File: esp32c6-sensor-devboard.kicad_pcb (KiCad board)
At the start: 4 copper layers, 90 x 50 mm, 183 parts, among them J1 Conn_01x04_Pin, J2 Micro_SD_Card_Det1, J3 Screw_Terminal_01x02, J4 USB_C_Receptacle_USB2.0_14P, J5 Screw_Terminal_01x02, J6 Screw_Terminal_01x06, J7 Screw_Terminal_01x04, J8 Conn_01x04_Pin, J9 Conn_01x03_Pin, SW1 SW_Push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

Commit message: pcb: add inner gnd planes
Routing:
- added copper zone on In1.Cu, net GND
- added copper zone on In2.Cu, net GND
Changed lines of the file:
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@@
+		)
+	)
+	(zone
+		(net 2)
+		(net_name "GND")
+		(layers "In1.Cu" "In2.Cu")
+		(hatch edge 0.5)
+		(connect_pads
+			(clearance 0.3)
+		)
+		(min_thickness 0.15)
+		(filled_areas_thickness no)
+		(fill yes
+			(thermal_gap 0.4)
+			(thermal_bridge_width 0.25)
+		)
+		(polygon
+			(pts
+				(xy 132 67) (xy 222 67) (xy 222 117) (xy 132 117)
+			)
 		)
 	)

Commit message: pcb: add tooling holes
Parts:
- added REF**: ToolingHole_1.152mm, MountingHole:ToolingHole_1.152mm, F.Cu at (216.0, 114.0)
- added REF**: ToolingHole_1.152mm, MountingHole:ToolingHole_1.152mm, F.Cu at (218.0, 70.0)
- added REF**: ToolingHole_1.152mm, MountingHole:ToolingHole_1.152mm, F.Cu at (151.0, 114.0)
- added REF**: ToolingHole_1.152mm, MountingHole:ToolingHole_1.152mm, F.Cu at (141.0, 75.0)

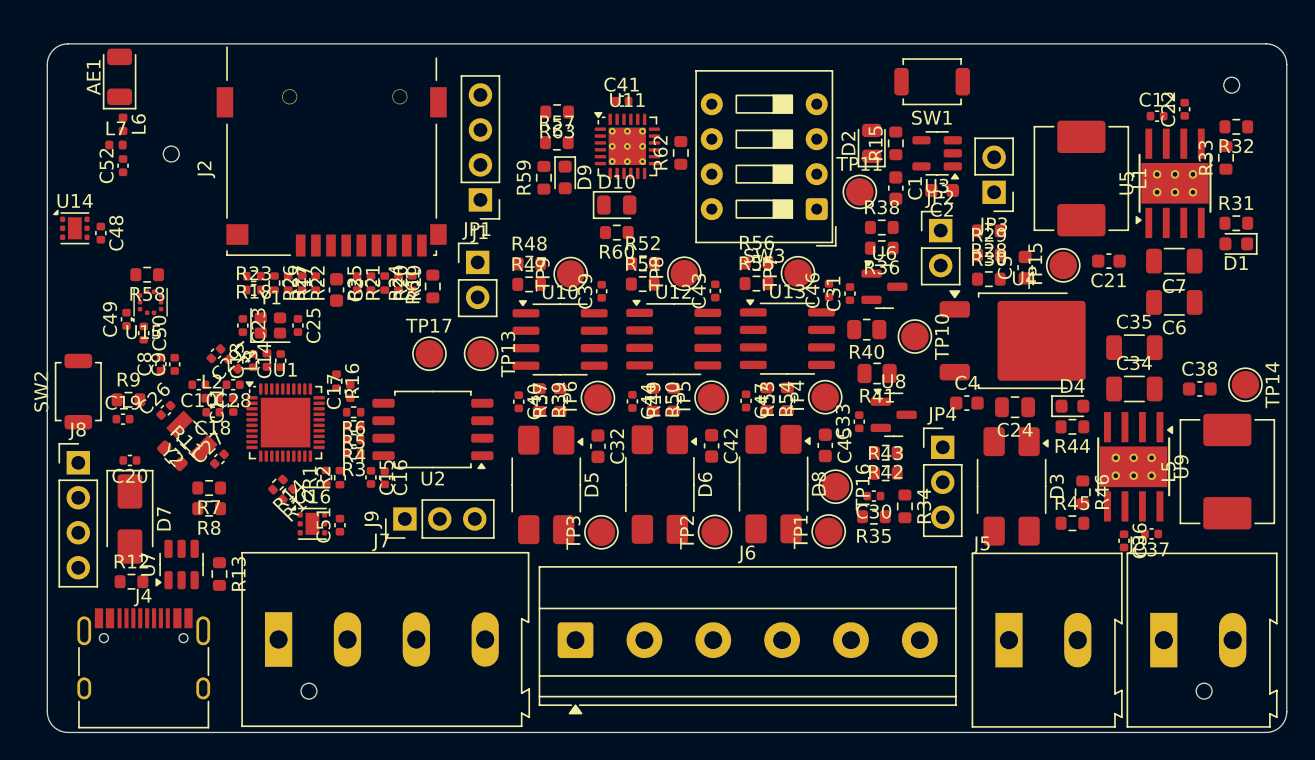
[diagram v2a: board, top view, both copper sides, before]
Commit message: pcb: add M2 mounting holes
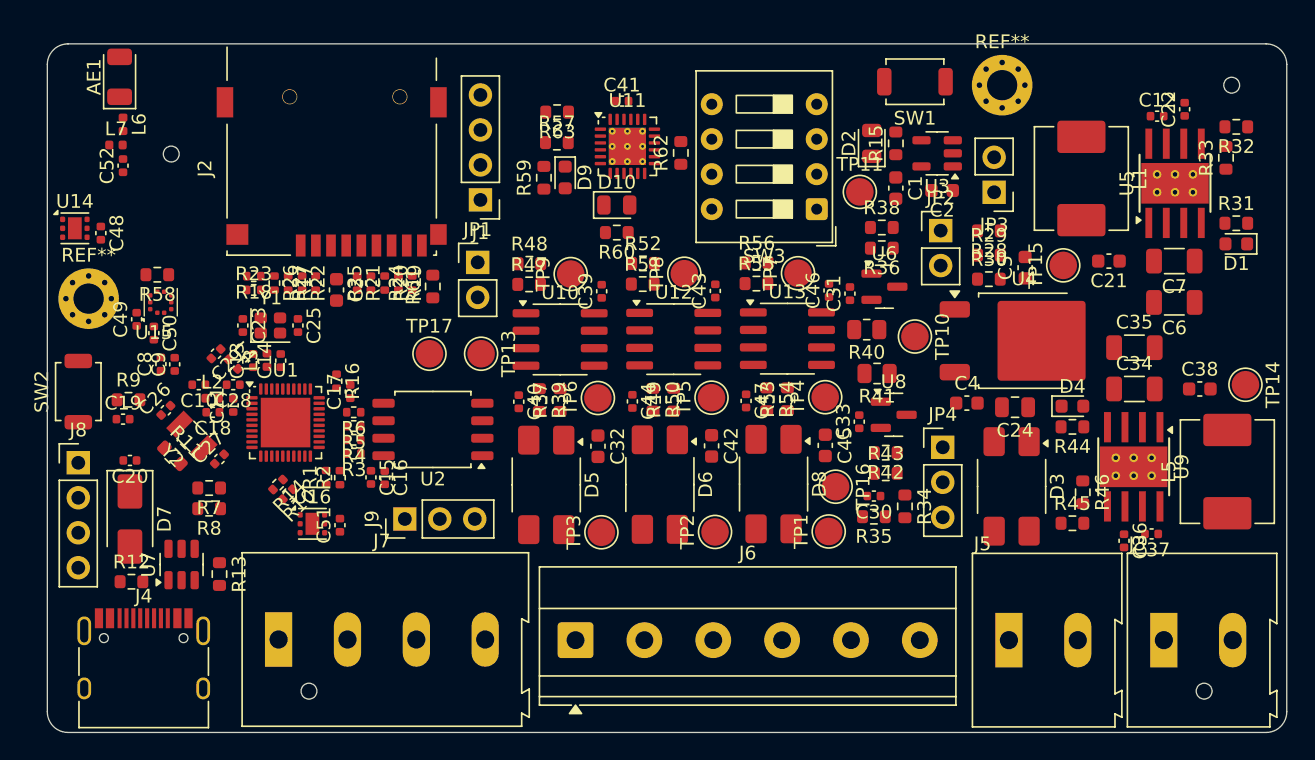
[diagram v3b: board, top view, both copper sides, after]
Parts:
- added REF**: MountingHole_2.2mm_M2_Pad_Via, MountingHole:MountingHole_2.2mm_M2_Pad_Via, F.Cu at (135.0, 85.5)
- added REF**: MountingHole_2.2mm_M2_Pad_Via, MountingHole:MountingHole_2.2mm_M2_Pad_Via, F.Cu at (201.3, 70.0)
- moved SW1 1.25 mm to (195.0, 69.8)
- moved C49 0.74 mm to (138.5, 87.0)
- moved C50 0.74 mm to (139.7, 88.0)
- moved R58 0.74 mm to (140.0, 83.8)
- moved U15 0.74 mm to (140.2, 85.8)

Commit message: pcb: add fiducials
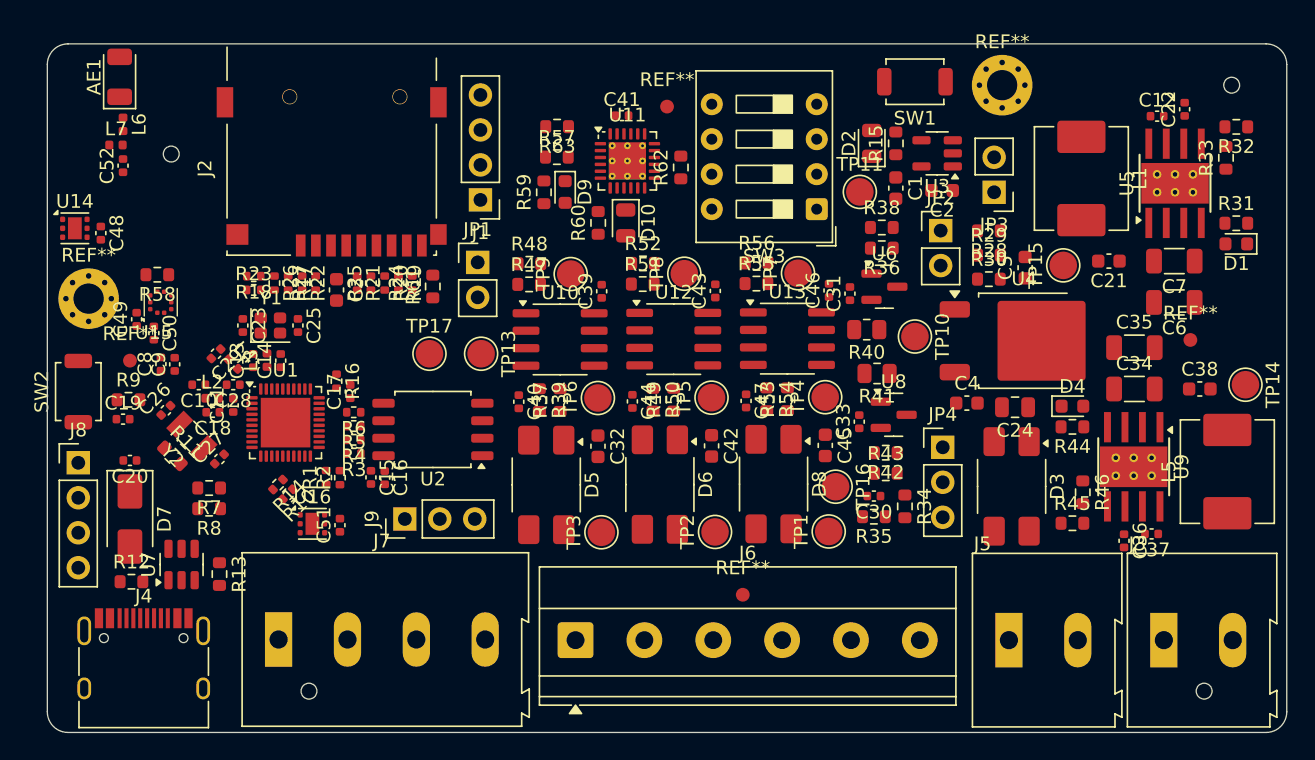
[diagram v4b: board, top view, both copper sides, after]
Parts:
- added REF**: Fiducial_1mm_Mask2mm, Fiducial:Fiducial_1mm_Mask2mm, F.Cu at (177.0, 71.6)
- added REF**: Fiducial_1mm_Mask2mm, Fiducial:Fiducial_1mm_Mask2mm, F.Cu at (215.0, 88.5)
- added REF**: Fiducial_1mm_Mask2mm, Fiducial:Fiducial_1mm_Mask2mm, F.Cu at (138.0, 90.0)
- added REF**: Fiducial_1mm_Mask2mm, Fiducial:Fiducial_1mm_Mask2mm, F.Cu at (182.5, 107.0)
- moved R60 1.52 mm to (172.0, 80.0), turned to 90 degrees
- moved D10 1.45 mm to (174.0, 80.0), turned to -90 degrees
- moved R59 1.06 mm to (168.1, 77.8)
- moved R63 1.06 mm to (169.0, 73.0)
- moved U11 1.06 mm to (174.1, 75.5)
- moved C41 1.05 mm to (173.7, 72.2)
- moved D9 1.05 mm to (169.6, 77.8)
- moved R57 1.05 mm to (169.0, 75.2)
- moved R62 1.05 mm to (178.0, 76.0)

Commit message: pcb: add gnd vias
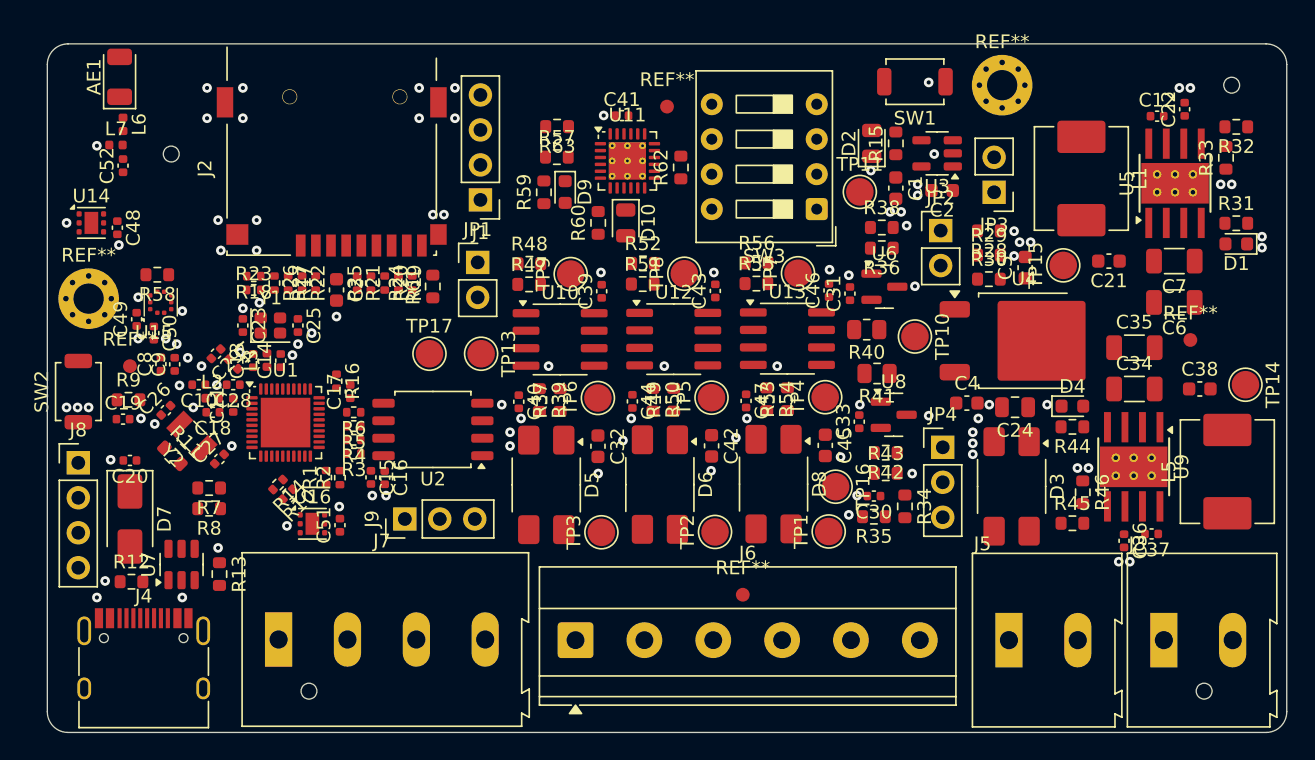
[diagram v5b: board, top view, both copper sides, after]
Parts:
- moved C48 1.26 mm to (137.1, 80.3)
- moved U14 1.26 mm to (135.2, 80.0)
- moved REF** 0.40 mm to (138.0, 90.4)
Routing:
- net GND: vias 0 -> 102

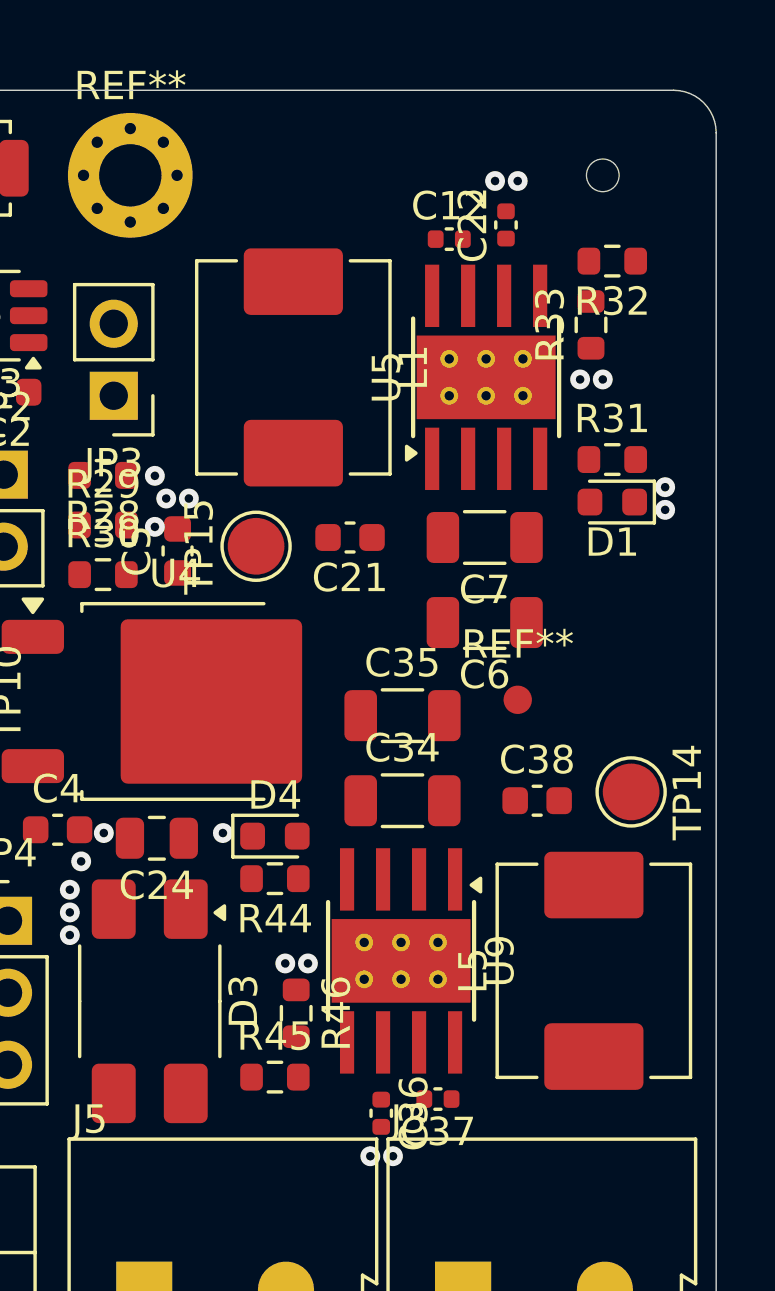
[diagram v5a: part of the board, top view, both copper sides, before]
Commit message: pcb: add smps routing
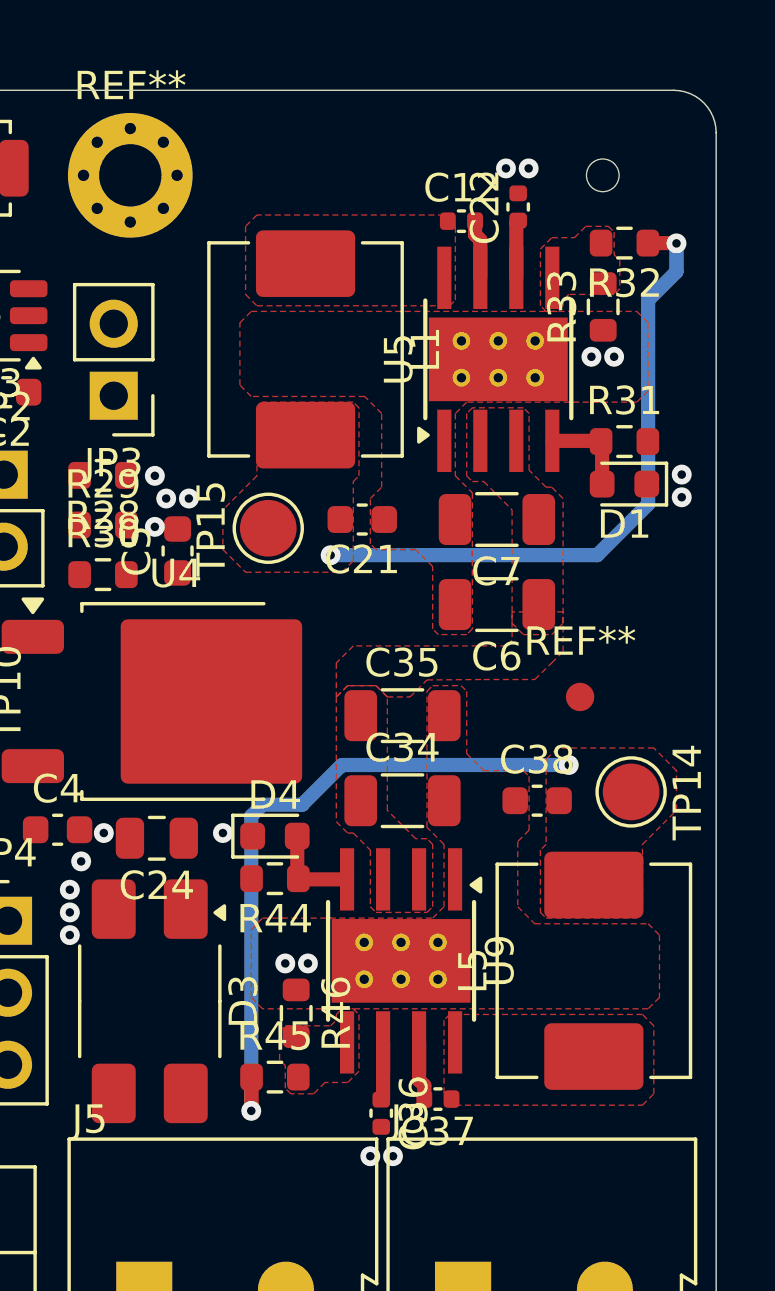
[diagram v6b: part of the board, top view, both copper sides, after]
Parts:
- moved REF** 2.20 mm to (217.2, 88.4)
- moved U5 0.77 mm to (214.3, 76.5)
- moved C21 0.77 mm to (209.5, 82.1)
- moved C6 0.77 mm to (214.3, 85.1)
- moved C7 0.77 mm to (214.3, 82.1)
- moved D1 0.77 mm to (218.8, 80.9)
- moved L1 0.77 mm to (207.5, 76.1)
- moved R31 0.77 mm to (218.8, 79.4)
- moved R32 0.77 mm to (218.8, 72.4)
- moved R33 0.77 mm to (218.0, 74.6)
- moved C12 0.77 mm to (213.0, 71.6)
- moved C22 0.77 mm to (215.0, 71.1)
- moved TP15 0.77 mm to (206.2, 82.5)
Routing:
- net /Power/+24VDC: track 0.00 -> 23.5 mm, vias 0 -> 2
- net Net-(JP3-A): track 0.00 -> 22.6 mm, vias 0 -> 2
- net Net-(D4-A): track 0.00 -> 3.25 mm
- net Net-(D1-A): track 0.00 -> 3.25 mm
- net Net-(U9-BOOT): track 0.00 -> 2.08 mm
- net Net-(U5-BOOT): track 0.00 -> 2.08 mm
- net Net-(U5-VCC): track 0.00 -> 2.05 mm
- net Net-(U9-VCC): track 0.00 -> 2.05 mm
- added copper zone on F.Cu, net +12/24DC
- added copper zone on F.Cu, net /Power/+24VDC
- added copper zone on F.Cu, net GND
- added copper zone on F.Cu, net Net-(JP3-A)
- added copper zone on F.Cu, net Net-(U5-FB)
- added copper zone on F.Cu, net Net-(U5-SW)
- added copper zone on F.Cu, net Net-(U9-FB)
- added copper zone on F.Cu, net Net-(U9-SW)
